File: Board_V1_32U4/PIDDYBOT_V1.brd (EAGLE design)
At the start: 48 x 76 mm, 58 parts, among them CN2 M02JST-PTH-2, U1 MPU-6050-1, U2 MCP73831, U4 TB6621FNG, U5 BLUETOOTH-RN41, U6 MIC5219, Y1 8Mhz

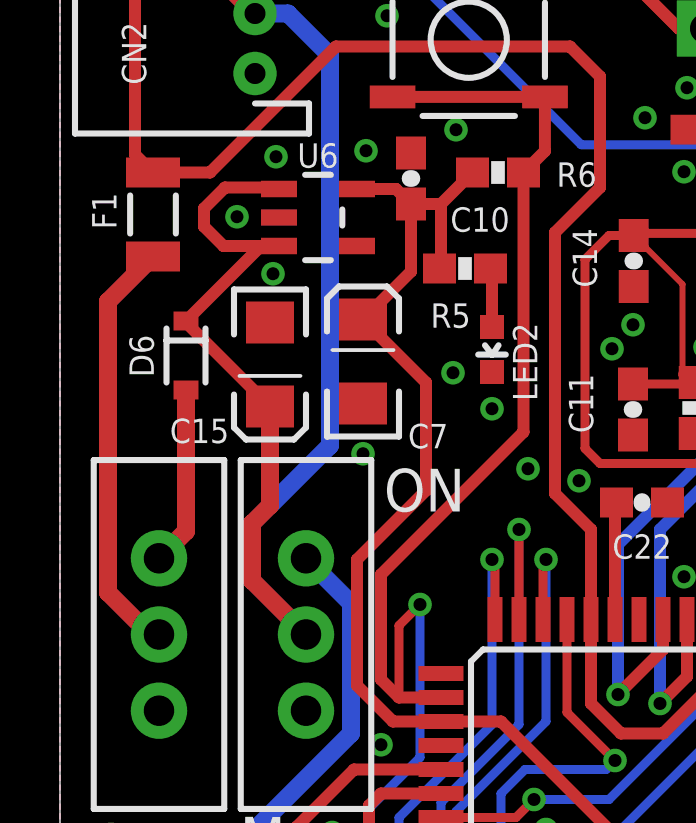
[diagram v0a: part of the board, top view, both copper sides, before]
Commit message: Changed power line for v_batt to v_motor
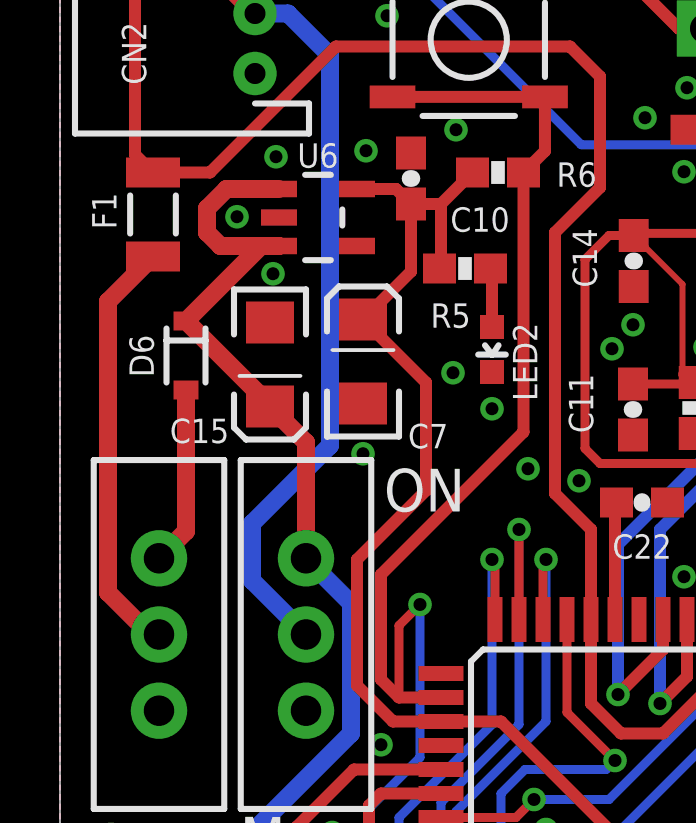
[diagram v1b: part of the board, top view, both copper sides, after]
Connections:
- net V_BATT: no longer C15.A, D6.1, U6.1, U6.3
- net V_MOTOR: now also C15.A, D6.1, U6.1, U6.3
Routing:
- net V_BATT: track 61.7 -> 38.8 mm
- net V_MOTOR: track 77.2 -> 97.0 mm
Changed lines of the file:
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@@
 <?xml version="1.0" encoding="utf-8"?>
 <!DOCTYPE eagle SYSTEM "eagle.dtd">
-<eagle version="6.5.0">
+<eagle version="7.1.0">
 <drawing>
 <settings>
@@
 <pass name="Default">
 <param name="RoutingGrid" value="50mil"/>
+<param name="AutoGrid" value="1"/>
+<param name="Efforts" value="0"/>
+<param name="TopRouterVariant" value="1"/>
 <param name="tpViaShape" value="round"/>
 <param name="PrefDir.1" value="|"/>
@@
 <contactref element="C6" pad="1"/>
 <wire x1="9.45" y1="67.0749" x2="9.475" y2="67.0499" width="0.4064" layer="1"/>
-<contactref element="U6" pad="1"/>
-<contactref element="U6" pad="3"/>
-<contactref element="C15" pad="A"/>
-<contactref element="D6" pad="1"/>
 <contactref element="S2" pad="2"/>
 <wire x1="9" y1="44.1" x2="9" y2="57.1" width="0.6" layer="16"/>
@@
 <wire x1="6.4" y1="41.5" x2="6.4" y2="39.6" width="0.6" layer="16"/>
 <wire x1="6.4" y1="39.6" x2="8.2" y2="37.8" width="0.6" layer="16"/>
-<wire x1="8.2" y1="37.8" x2="6.4" y2="39.6" width="0.6" layer="1"/>
-<wire x1="6.4" y1="39.6" x2="6.4" y2="41.5" width="0.6" layer="1"/>
-<wire x1="6.4" y1="41.5" x2="7" y2="42.1" width="0.6" layer="1"/>
-<wire x1="7" y1="42.1" x2="7" y2="45.4" width="0.6" layer="1"/>
-<wire x1="7" y1="45.4" x2="4.2" y2="48.2" width="0.4" layer="1"/>
-<wire x1="4.2" y1="48.2" x2="4.2" y2="48.25" width="0.4" layer="1"/>
-<wire x1="4.2" y1="48.25" x2="6.7" y2="50.75" width="0.4" layer="1"/>
-<wire x1="6.7" y1="50.75" x2="7.2999" y2="50.75" width="0.4" layer="1"/>
-<wire x1="7.2999" y1="50.75" x2="5.45" y2="50.75" width="0.4" layer="1"/>
-<wire x1="5.45" y1="50.75" x2="4.8" y2="51.4" width="0.4" layer="1"/>
-<wire x1="4.8" y1="51.4" x2="4.8" y2="52" width="0.4" layer="1"/>
-<wire x1="4.8" y1="52" x2="5.5" y2="52.7" width="0.4" layer="1"/>
-<wire x1="5.5" y1="52.7" x2="7.2499" y2="52.7" width="0.4" layer="1"/>
-<wire x1="7.2499" y1="52.7" x2="7.2999" y2="52.65" width="0.4" layer="1"/>
 <wire x1="9.475" y1="67.0499" x2="9.475" y2="65.575" width="0.4" layer="1"/>
 <wire x1="9.475" y1="65.575" x2="9.275" y2="65.375" width="0.4" layer="1"/>
@@
 <wire x1="14.6" y1="22" x2="17.5" y2="22" width="0.6" layer="16"/>
 <wire x1="17.5" y1="22" x2="18.1" y2="21.4" width="0.6" layer="16"/>
+<contactref element="D6" pad="1"/>
+<contactref element="U6" pad="1"/>
+<contactref element="C15" pad="A"/>
+<contactref element="U6" pad="3"/>
+<wire x1="8.2" y1="40.34" x2="8.2" y2="44.2" width="0.6" layer="1"/>
+<wire x1="8.2" y1="44.2" x2="7" y2="45.4" width="0.6" layer="1"/>
+<wire x1="7" y1="45.4" x2="7" y2="45.45" width="0.6" layer="1"/>
+<wire x1="7" y1="45.45" x2="4.2" y2="48.25" width="0.6" layer="1"/>
+<wire x1="4.2" y1="48.25" x2="6.7" y2="50.75" width="0.6" layer="1"/>
+<wire x1="6.7" y1="50.75" x2="7.2999" y2="50.75" width="0.6" layer="1"/>
+<wire x1="7.2999" y1="50.75" x2="5.35" y2="50.75" width="0.6" layer="1"/>
+<wire x1="5.35" y1="50.75" x2="4.9" y2="51.2" width="0.6" layer="1"/>
+<wire x1="4.9" y1="51.2" x2="4.9" y2="52" width="0.6" layer="1"/>
+<wire x1="4.9" y1="52" x2="5.55" y2="52.65" width="0.6" layer="1"/>
+<wire x1="5.55" y1="52.65" x2="7.2999" y2="52.65" width="0.6" layer="1"/>
 </signal>
 <signal name="N$3">

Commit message: latest PIDDYBOT 32u4 update
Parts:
- removed S2, S3: (no value), SparkFun-Electromechanical:SWITCH-SPDT
- added C1: 1uF, SparkFun:0603-CAP
- added L2: 33uH, SparkFun-Passives:C0402
- added LOGO1: IDLEHANDS_LOGOL, IdleHandsProject:IHD-LOGO-L
- added LOGO2: OSHW-LOGOM, SparkFun-Aesthetics:OSHW-LOGO-M
- added R1: 1M, SparkFun:0603-RES
- added R3: 470k, SparkFun:0603-RES
- added S4: (no value), SparkFun-Electromechanical:SWITCH-SPDT
- moved C11 8.13 mm to (11.2, 43.4), turned to 0 degrees
- moved R10 4.19 mm to (24.9, 43.4), turned to 180 degrees
- moved C9 0.40 mm to (21.8, 55.0)
- moved C16 0.30 mm to (25.8, 55.0)
- moved C14 0.20 mm to (19.3, 50.2)
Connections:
- removed net D11: U$1.12
- removed net N$4: D6.2, S3.3
- removed net VIO: C16.1, U1.8
- removed net V_MOTOR: C15.A, C17.1, C19.A, D6.1, S2.3, U4.13, U4.14, U4.24, U6.1, U6.3
- new net BATT: C1.1, R1.1, R3.2
- new net ISOLATEDVCC: C14.1, C16.1, L2.2, U1.13, U1.8
- new net RAW: C15.A, C17.1, C19.A, D6.1, R1.2, S4.2, U4.13, U4.14, U4.24, U6.1, U6.3
- net 3.3V: now also L2.1; no longer C14.1, U1.13
- net AIN1: now also U$1.31; no longer U$1.32
- net AIN2: now also U$1.26; no longer U$1.30
- net GND: now also C1.2, R3.1, U1.1, U1.11
- net INT: now also U$1.12
- net MTE_A_2: now also U$1.30; no longer U$1.26
- net N$3: now also D6.2; no longer S3.2
- net PWMB: now also U$1.32; no longer U$1.31
- net V_BATT: now also S4.1; no longer S2.2
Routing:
- net V_MOTOR: track 97.0 -> 0.00 mm, vias 1 -> 0
- net RAW: track 0.00 -> 94.8 mm, vias 0 -> 1
- net INT: track 0.00 -> 23.9 mm, vias 0 -> 2
- net 3.3V: track 298.3 -> 276.7 mm
- net ISOLATEDVCC: track 0.00 -> 17.8 mm
- net PWMB: track 15.4 -> 4.82 mm, vias 2 -> 1
- net MTE_A_2: track 18.6 -> 9.07 mm, vias 1 -> 0
- net N$3: track 14.1 -> 4.91 mm
- net AIN2: track 9.13 -> 0.00 mm
- net AIN1: track 8.77 -> 0.04 mm
- net N$4: track 5.98 -> 0.00 mm
- net SCL: track 30.9 -> 25.0 mm
- net GND: track 0.00 -> 5.29 mm, vias 90 -> 94
- net V_BATT: track 38.8 -> 35.0 mm
- net VIO: track 2.81 -> 0.00 mm
- added copper zone on layer 1, net N$5
- added copper zone on layer 16, net N$5
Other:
- board text added: "#PIDDYBOT_V1"
- board text added: "IDLE HANDS DEV."
- board text removed: "A"
- board text removed: "M"
